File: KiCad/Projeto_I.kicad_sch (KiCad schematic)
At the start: 4 parts, among them U1 PIC18F4550-IP, Y1 16MHz

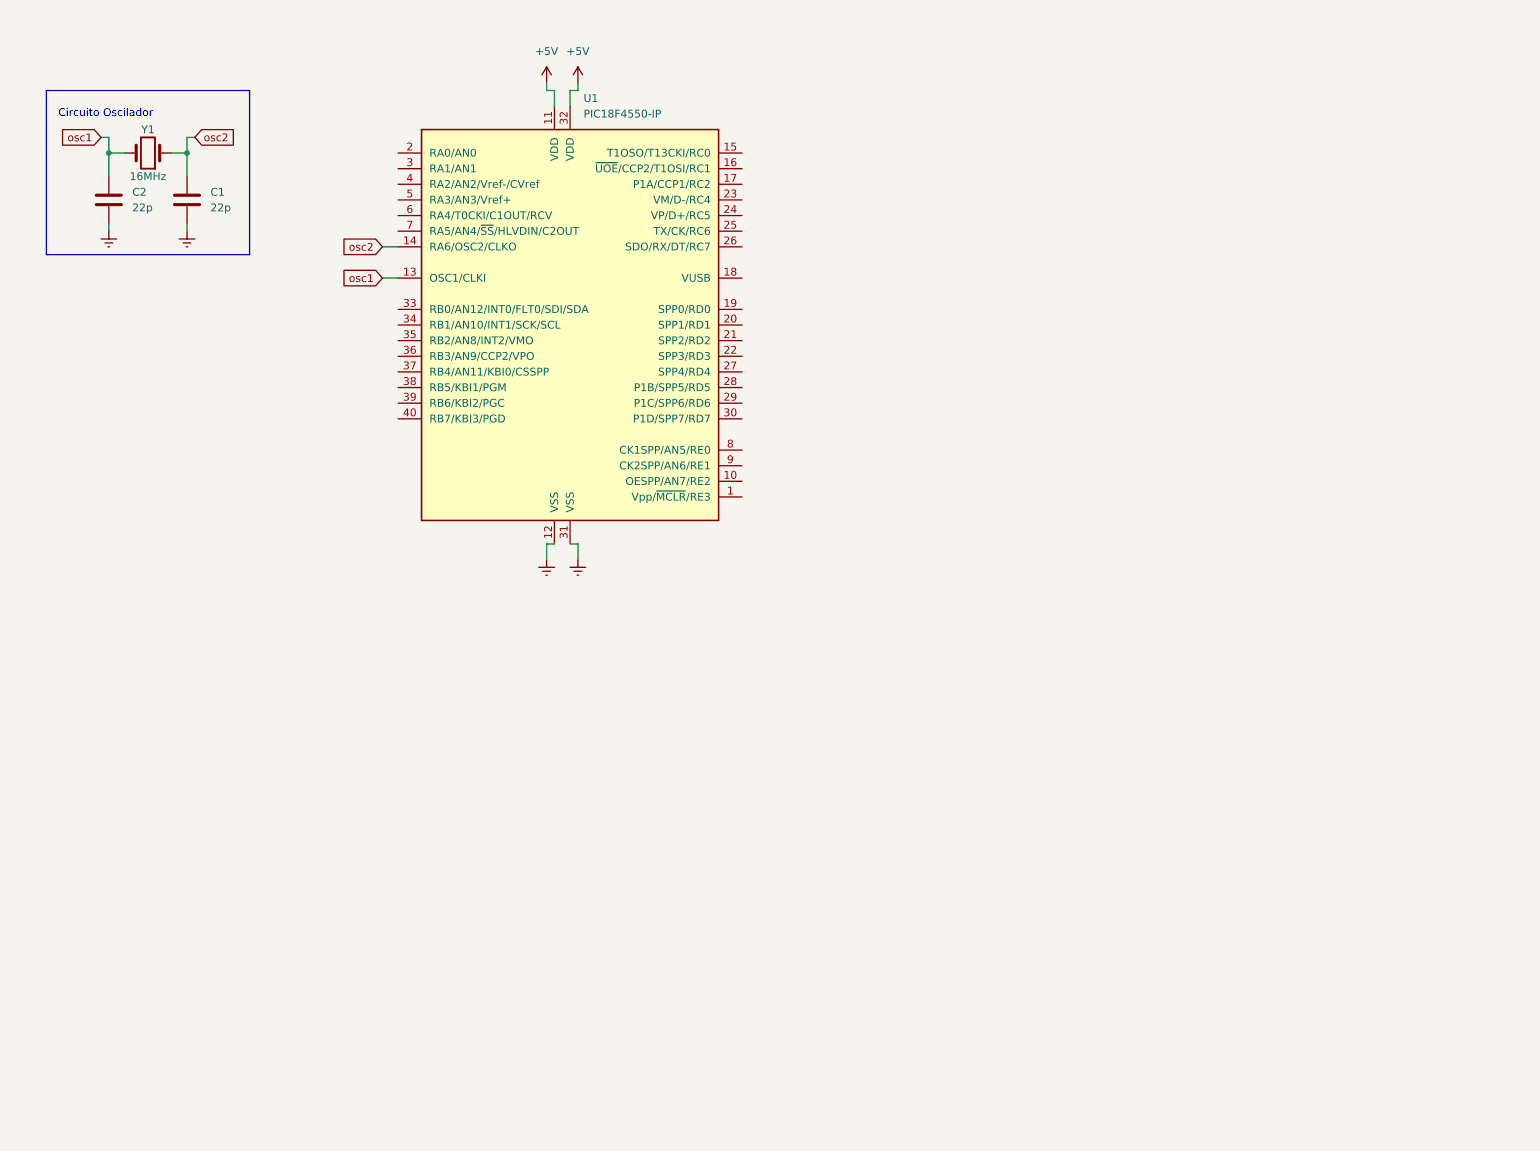
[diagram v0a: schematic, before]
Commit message: Integração das portas de entradas e saidas
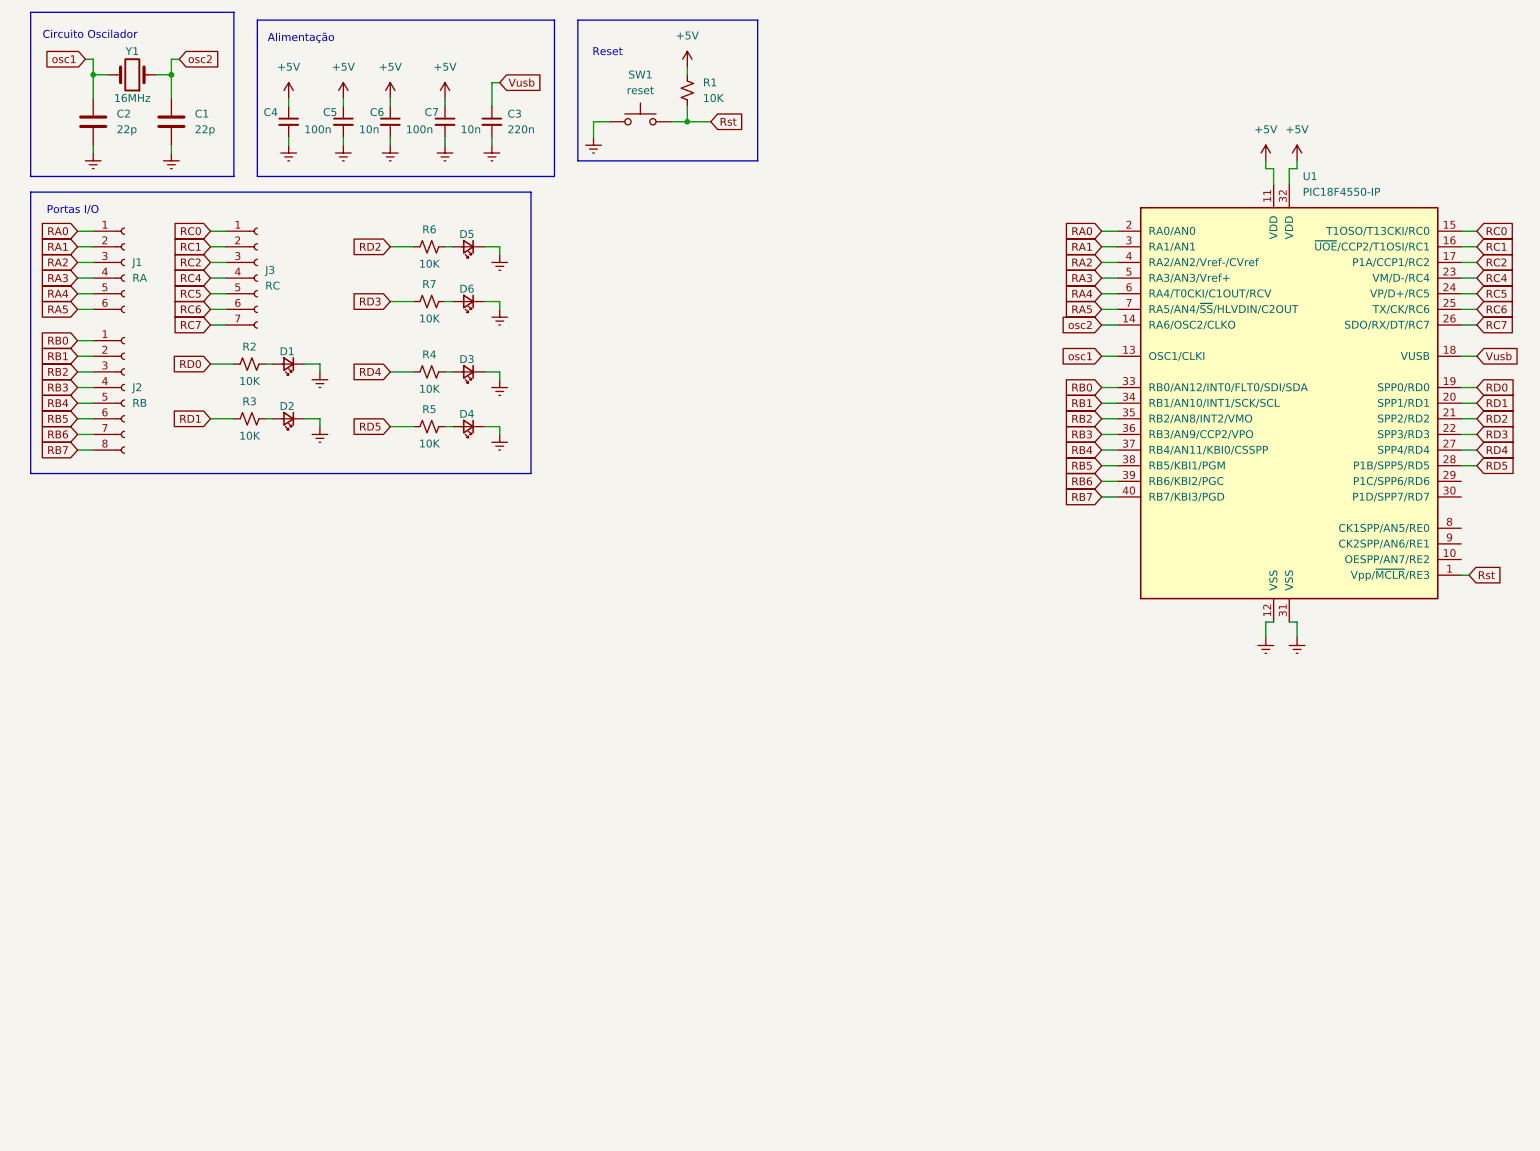
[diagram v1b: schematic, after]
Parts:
- added C3: 220n, Capacitor_THT:C_Rect_L7.0mm_W2.5mm_P5.00mm, symbol Device:C_Small
- added C4, C6: 100n, Capacitor_THT:C_Rect_L7.0mm_W2.5mm_P5.00mm, symbol Device:C_Small
- added C5, C7: 10n, Capacitor_THT:C_Rect_L7.0mm_W2.5mm_P5.00mm, symbol Device:C_Small
- added D1, D2, D3, D4, D5, D6: RD0, LED_THT:LED_D3.0mm, symbol Device:LED_Small
- added J1: RA, Connector_PinSocket_2.54mm:PinSocket_1x06_P2.54mm_Vertical, symbol Connector:Conn_01x06_Socket
- added J2: RB, Connector_PinSocket_2.54mm:PinSocket_1x08_P2.54mm_Vertical, symbol Connector:Conn_01x08_Socket
- added J3: RC, Connector_PinSocket_2.54mm:PinSocket_1x07_P2.54mm_Vertical, symbol Connector:Conn_01x07_Socket
- added R1, R2, R3, R4, R5, R6, R7: 10K, Resistor_THT:R_Axial_DIN0207_L6.3mm_D2.5mm_P7.62mm_Horizontal, symbol Device:R_Small_US
- added SW1: reset, Button_Switch_THT:SW_TH_Tactile_Omron_B3F-10xx, symbol Switch:SW_Push
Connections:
- net +5V: now also C4.1, C5.1, C6.1, C7.1, R1.1
- net Earth: now also C3.2, C4.2, C5.2, C6.2, C7.2, D1.1 (K), D2.1 (K), D3.1 (K), D4.1 (K), D5.1 (K), D6.1 (K), SW1.1
- net Rst: now reaches U1.1 (Vpp/~{MCLR}/RE3)
- net Rst: now also R1.2, SW1.2
- net RC0: now reaches U1.15 (T1OSO/T13CKI/RC0)
- net RC0: now also J3.1 (Pin_1)
- net RC1: now reaches U1.16 (~{UOE}/CCP2/T1OSI/RC1)
- net RC1: now also J3.2 (Pin_2)
- net RC2: now reaches U1.17 (P1A/CCP1/RC2)
- net RC2: now also J3.3 (Pin_3)
- net Vusb: now reaches U1.18 (VUSB)
- net Vusb: now also C3.1
- net RD0: now reaches U1.19 (SPP0/RD0)
- net RD0: now also R2.1
- net RA0: now reaches U1.2 (RA0/AN0)
- net RA0: now also J1.1 (Pin_1)
- net RD1: now reaches U1.20 (SPP1/RD1)
- net RD1: now also R3.1
- net RD2: now reaches U1.21 (SPP2/RD2)
- net RD2: now also R6.1
- net RD3: now reaches U1.22 (SPP3/RD3)
- net RD3: now also R7.1
- net RC4: now reaches U1.23 (VM/D-/RC4)
- net RC4: now also J3.4 (Pin_4)
- net RC5: now reaches U1.24 (VP/D+/RC5)
- net RC5: now also J3.5 (Pin_5)
- net RC6: now reaches U1.25 (TX/CK/RC6)
- net RC6: now also J3.6 (Pin_6)
- net RC7: now reaches U1.26 (SDO/RX/DT/RC7)
- net RC7: now also J3.7 (Pin_7)
- net RD4: now reaches U1.27 (SPP4/RD4)
- net RD4: now also R4.1
- net RD5: now reaches U1.28 (P1B/SPP5/RD5)
- net RD5: now also R5.1
- net RA1: now reaches U1.3 (RA1/AN1)
- net RA1: now also J1.2 (Pin_2)
- net RB0: now reaches U1.33 (RB0/AN12/INT0/FLT0/SDI/SDA)
- net RB0: now also J2.1 (Pin_1)
- net RB1: now reaches U1.34 (RB1/AN10/INT1/SCK/SCL)
- net RB1: now also J2.2 (Pin_2)
- net RB2: now reaches U1.35 (RB2/AN8/INT2/VMO)
- net RB2: now also J2.3 (Pin_3)
- net RB3: now reaches U1.36 (RB3/AN9/CCP2/VPO)
- net RB3: now also J2.4 (Pin_4)
- net RB4: now reaches U1.37 (RB4/AN11/KBI0/CSSPP)
- net RB4: now also J2.5 (Pin_5)
- net RB5: now reaches U1.38 (RB5/KBI1/PGM)
- net RB5: now also J2.6 (Pin_6)
- net RB6: now reaches U1.39 (RB6/KBI2/PGC)
- net RB6: now also J2.7 (Pin_7)
- net RA2: now reaches U1.4 (RA2/AN2/Vref-/CVref)
- net RA2: now also J1.3 (Pin_3)
- net RB7: now reaches U1.40 (RB7/KBI3/PGD)
- net RB7: now also J2.8 (Pin_8)
- net RA3: now reaches U1.5 (RA3/AN3/Vref+)
- net RA3: now also J1.4 (Pin_4)
- net RA4: now reaches U1.6 (RA4/T0CKI/C1OUT/RCV)
- net RA4: now also J1.5 (Pin_5)
- net RA5: now reaches U1.7 (RA5/AN4/~{SS}/HLVDIN/C2OUT)
- net RA5: now also J1.6 (Pin_6)
- new net: D4.2 (A), R5.2
- new net: D3.2 (A), R4.2
- new net: D2.2 (A), R3.2
- new net: D1.2 (A), R2.2
- new net: D6.2 (A), R7.2
- new net: D5.2 (A), R6.2
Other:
- note added: "Alimentação"
- note added: "Portas I/O"
- note added: "Reset"
- moved on the sheet: C1, C2, U1, Y1

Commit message: Inclusão dos módulos de alimentação e comutação
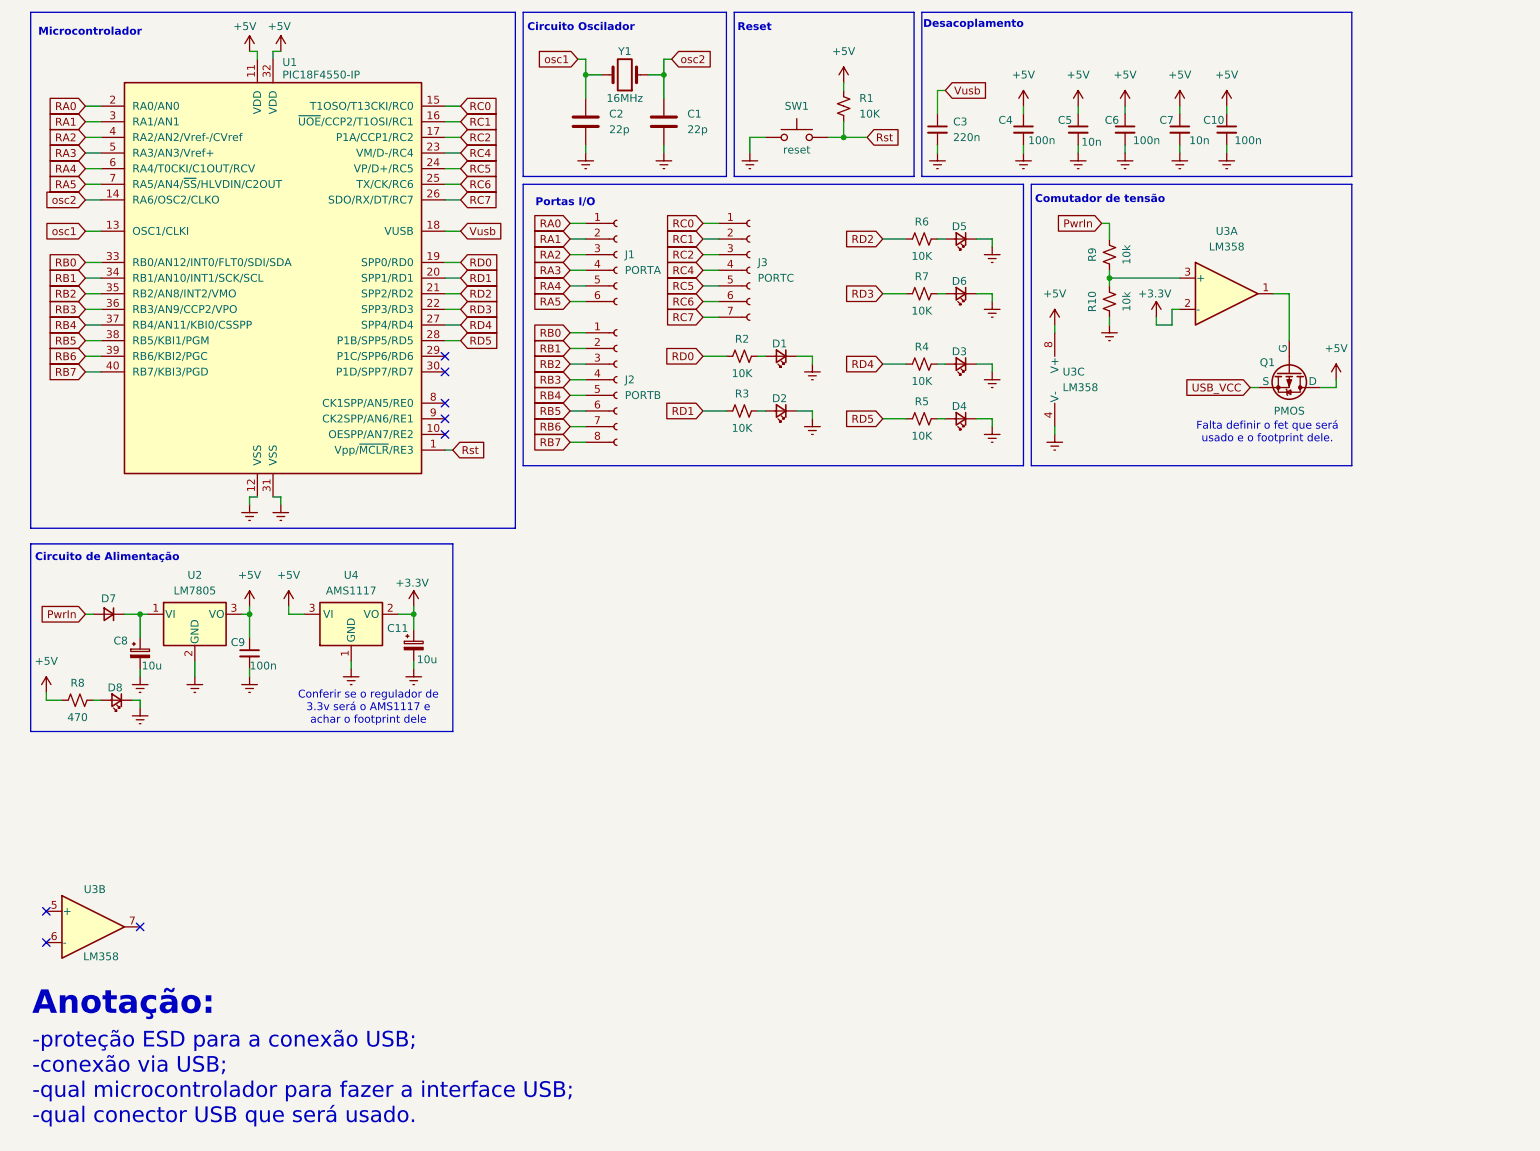
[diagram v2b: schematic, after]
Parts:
- added C10, C9: 100n, Capacitor_THT:C_Rect_L7.0mm_W2.5mm_P5.00mm, symbol Device:C_Small
- added C11, C8: 10u, symbol Device:C_Polarized_Small
- added D7: D_Small, symbol Device:D_Small
- added D8: RD0, LED_THT:LED_D3.0mm, symbol Device:LED_Small
- added Q1: PMOS, symbol Simulation_SPICE:PMOS
- added R10, R9: 10k, Resistor_THT:R_Axial_DIN0207_L6.3mm_D2.5mm_P7.62mm_Horizontal, symbol Device:R_Small_US
- added R8: 470, Resistor_THT:R_Axial_DIN0207_L6.3mm_D2.5mm_P7.62mm_Horizontal, symbol Device:R_Small_US
- added U2: LM7805, Package_TO_SOT_THT:TO-220-3_Horizontal_TabDown, symbol Regulator_Linear:LM7805_TO220
- added U3: LM358, Package_DIP:DIP-8_W7.62mm, symbol Amplifier_Operational:LM358
- added U4: AMS1117, symbol Regulator_Linear:AMS1117-3.3
- J1: value RA -> PORTA
- J2: value RB -> PORTB
- J3: value RC -> PORTC
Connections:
- net +5V: now also C10.1, C9.1, Q1.1 (D), R8.1, U2.3 (VO), U3.8 (V+), U4.3 (VI)
- net Earth: now also C10.2, C11.2, C8.2, C9.2, D8.1 (K), R10.1, U2.2 (GND), U3.4 (V-), U4.1 (GND)
- new net: D8.2 (A), R8.2
- new net: R10.2, R9.1, U3.3 (+)
- new net: Q1.2 (G), U3.1
- new net: C8.1, D7.1 (K), U2.1 (VI)
- new net +3.3V: C11.1, U3.2 (-), U4.2 (VO)
- new net PwrIn: D7.2 (A), R9.2
- new net USB_VCC: Q1.3 (S)
- no-connect marks 0 -> 8
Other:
- note added: "-proteção ESD para a conexão USB; -conexão via USB; -qual microcontrolador para fazer a interface USB; -qual conector USB que será usado."
- note added: "Anotação:"
- note added: "Circuito de Alimentação"
- note added: "Comutador de tensão"
- note added: "Conferir se o regulador de 3.3v será o AMS1117 e achar o footprint dele"
- note added: "Desacoplamento"
- note added: "Falta definir o fet que será usado e o footprint dele."
- note added: "Microcontrolador"
- note removed: "Alimentação"
- moved on the sheet: C1, C2, C3, C4, C5, C6, C7, D1, D2, D3, D4, D5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

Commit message: Aula do dia 28/03
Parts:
- added J4: USB_B_Micro, Connector_USB:USB_Micro-AB_Molex_47590-0001, symbol Connector:USB_B_Micro
- added J5: Barrel_Jack_Switch, Connector_BarrelJack:BarrelJack_Horizontal, symbol Connector:Barrel_Jack_Switch
- D7: footprint (none) -> Diode_THT:D_DO-41_SOD81_P10.16mm_Horizontal
- U2: footprint Package_TO_SOT_THT:TO-220-3_Horizontal_TabDown -> Package_TO_SOT_THT:TO-220-3_Vertical
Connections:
- net Earth: now also J4.5 (GND), J4.6 (Shield), J5.2, J5.3
- net PwrIn: now also J5.1
- net RC4: now also J4.2 (D-)
- net RC5: now also J4.3 (D+)
- no-connect marks 8 -> 9

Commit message: AUla do dia 04/04/2025
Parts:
- added F1: MF-MSMF050-2, Library:FUSM4632X85, symbol MF-MSMF050-2:MF-MSMF050-2
- C1: footprint Capacitor_THT:C_Disc_D7.5mm_W5.0mm_P7.50mm -> Capacitor_THT:C_Rect_L7.0mm_W2.5mm_P5.00mm
- C11, C8: footprint (none) -> Capacitor_THT:CP_Radial_D10.0mm_P3.80mm
- C2: footprint (none) -> Capacitor_THT:C_Rect_L7.0mm_W2.5mm_P5.00mm
- Q1: footprint (none) -> Package_TO_SOT_THT:TO-92L_HandSolder
- U4: footprint (none) -> Package_TO_SOT_SMD:SOT-223-3_TabPin2
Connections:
- net +5V: now also F1.2
- net at J4.1 (VBUS): now also F1.1
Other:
- note added: "-proteção ESD para a conexão USB;"
- note removed: "-proteção ESD para a conexão USB; -conexão via USB; -qual microcontrolador para fazer a interface USB; -qual conector USB que será usado."
- note removed: "Conferir se o regulador de 3.3v será o AMS1117 e achar o footprint dele"
- moved on the sheet: J4, J5, U3B
